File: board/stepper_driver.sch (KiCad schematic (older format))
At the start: 10 parts

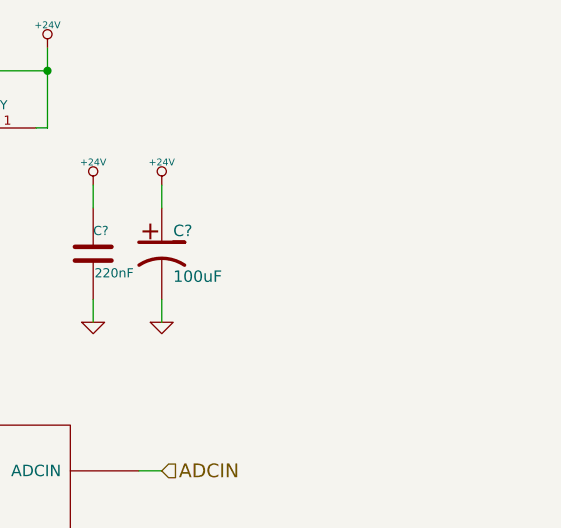
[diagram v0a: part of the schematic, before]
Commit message: Reiner Documentation, Industrial GPIO, Driver Fix
I added documentation for the meaning of Reiner's board pins. I have
finished implemented the industrial inputs on the schematic and partial
industrial outputs. I have added some capacitors to the motor drivers.
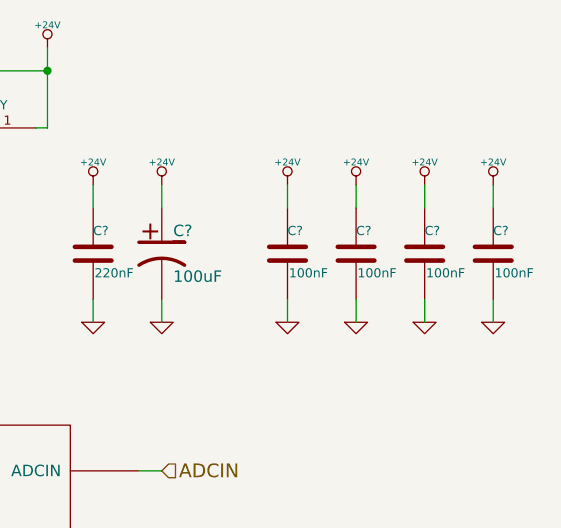
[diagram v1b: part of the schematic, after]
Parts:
- added C? (x4): 100nF, symbol C
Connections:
- net +24V: now also C?.1, C?.1, C?.1, C?.1
- net GND: now also C?.2, C?.2, C?.2, C?.2
- new net: J?.~ (2B), U?.~ (~STBY/RST) (x3)
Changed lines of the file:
@@
 $Descr USLetter 11000 8500
 encoding utf-8
-Sheet 4 10
+Sheet 2 26
 Title "L64470 Stepper Driver"
 Date "21 jan 2014"
@@
 Wire Wire Line
 	6550 3850 6650 3850
+$Comp
+L GND #PWR?
+U 1 1 52FDE021
+P 7200 3200
+F 0 "#PWR?" H 7200 3200 30  0001 C CNN
+F 1 "GND" H 7200 3130 30  0001 C CNN
+F 2 "" H 7200 3200 60  0000 C CNN
+F 3 "" H 7200 3200 60  0000 C CNN
+	1    7200 3200
+	1    0    0    -1
+$EndComp
+$Comp
+L +24V #PWR?
+U 1 1 52FDE027
+P 7200 2600
+F 0 "#PWR?" H 7200 2550 20  0001 C CNN
+F 1 "+24V" H 7200 2700 30  0000 C CNN
+F 2 "" H 7200 2600 60  0000 C CNN
+F 3 "" H 7200 2600 60  0000 C CNN
+	1    7200 2600
+	1    0    0    -1
+$EndComp
+$Comp
+L C C?
+U 1 1 52FDE02D
+P 7200 2900
+F 0 "C?" H 7200 3000 40  0000 L CNN
+F 1 "100nF" H 7206 2815 40  0000 L CNN
+F 2 "" H 7238 2750 30  0000 C CNN
+F 3 "" H 7200 2900 60  0000 C CNN
+	1    7200 2900
+	1    0    0    -1
+$EndComp
+Wire Wire Line
+	7200 2600 7200 2700
+Wire Wire Line
+	7200 3100 7200 3200
+$Comp
+L GND #PWR?
+U 1 1 52FDE03A
+P 7500 3200
+F 0 "#PWR?" H 7500 3200 30  0001 C CNN
+F 1 "GND" H 7500 3130 30  0001 C CNN
+F 2 "" H 7500 3200 60  0000 C CNN
+F 3 "" H 7500 3200 60  0000 C CNN
+	1    7500 3200
+	1    0    0    -1
+$EndComp
+$Comp
+L +24V #PWR?
+U 1 1 52FDE040
+P 7500 2600
+F 0 "#PWR?" H 7500 2550 20  0001 C CNN
+F 1 "+24V" H 7500 2700 30  0000 C CNN
+F 2 "" H 7500 2600 60  0000 C CNN
+F 3 "" H 7500 2600 60  0000 C CNN
+	1    7500 2600
+	1    0    0    -1
+$EndComp
+$Comp
+L C C?
+U 1 1 52FDE046
+P 7500 2900
+F 0 "C?" H 7500 3000 40  0000 L CNN
+F 1 "100nF" H 7506 2815 40  0000 L CNN
+F 2 "" H 7538 2750 30  0000 C CNN
+F 3 "" H 7500 2900 60  0000 C CNN
+	1    7500 2900
+	1    0    0    -1
+$EndComp
+Wire Wire Line
+	7500 2600 7500 2700
+Wire Wire Line
+	7500 3100 7500 3200
+$Comp
+L GND #PWR?
+U 1 1 52FDE04E
+P 7800 3200
+F 0 "#PWR?" H 7800 3200 30  0001 C CNN
+F 1 "GND" H 7800 3130 30  0001 C CNN
+F 2 "" H 7800 3200 60  0000 C CNN
+F 3 "" H 7800 3200 60  0000 C CNN
+	1    7800 3200
+	1    0    0    -1
+$EndComp
+$Comp
+L +24V #PWR?
+U 1 1 52FDE054
+P 7800 2600
+F 0 "#PWR?" H 7800 2550 20  0001 C CNN
+F 1 "+24V" H 7800 2700 30  0000 C CNN
+F 2 "" H 7800 2600 60  0000 C CNN
+F 3 "" H 7800 2600 60  0000 C CNN
+	1    7800 2600
+	1    0    0    -1
+$EndComp
+$Comp
+L C C?
+U 1 1 52FDE05A
+P 7800 2900
+F 0 "C?" H 7800 3000 40  0000 L CNN
+F 1 "100nF" H 7806 2815 40  0000 L CNN
+F 2 "" H 7838 2750 30  0000 C CNN
+F 3 "" H 7800 2900 60  0000 C CNN
+	1    7800 2900
+	1    0    0    -1
+$EndComp
+Wire Wire Line
+	7800 2600 7800 2700
+Wire Wire Line
+	7800 3100 7800 3200
+$Comp
+L GND #PWR?
+U 1 1 52FDE062
+P 8100 3200
+F 0 "#PWR?" H 8100 3200 30  0001 C CNN
+F 1 "GND" H 8100 3130 30  0001 C CNN
+F 2 "" H 8100 3200 60  0000 C CNN
+F 3 "" H 8100 3200 60  0000 C CNN
+	1    8100 3200
+	1    0    0    -1
+$EndComp
+$Comp
+L +24V #PWR?
+U 1 1 52FDE068
+P 8100 2600
+F 0 "#PWR?" H 8100 2550 20  0001 C CNN
+F 1 "+24V" H 8100 2700 30  0000 C CNN
+F 2 "" H 8100 2600 60  0000 C CNN
+F 3 "" H 8100 2600 60  0000 C CNN
+	1    8100 2600
+	1    0    0    -1
+$EndComp
+$Comp
+L C C?
+U 1 1 52FDE06E
+P 8100 2900
+F 0 "C?" H 8100 3000 40  0000 L CNN
+F 1 "100nF" H 8106 2815 40  0000 L CNN
+F 2 "" H 8138 2750 30  0000 C CNN
+F 3 "" H 8100 2900 60  0000 C CNN
+	1    8100 2900
+	1    0    0    -1
+$EndComp
+Wire Wire Line
+	8100 2600 8100 2700
+Wire Wire Line
+	8100 3100 8100 3200
 $EndSCHEMATC

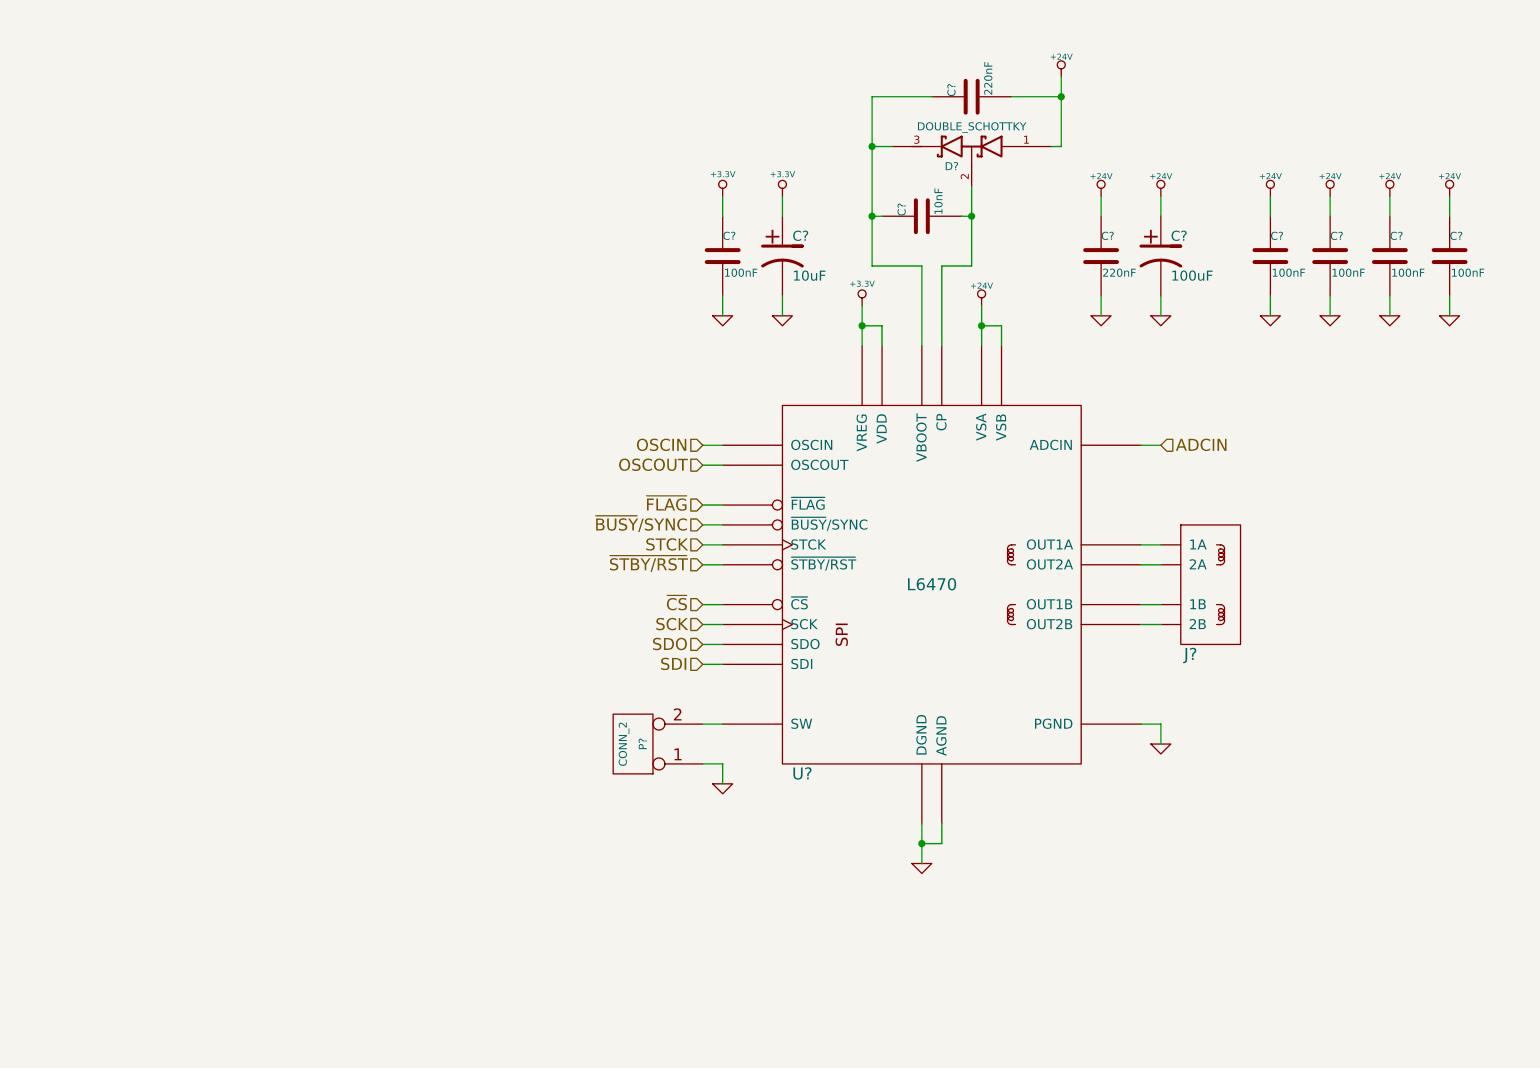
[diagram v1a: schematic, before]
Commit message: Decoupled the Stepper Driver, Main Schematic
The stepper driver is now decoupled according to the demo board
schematic.

The main schematic is nearly complete minus a couple of minor issues.
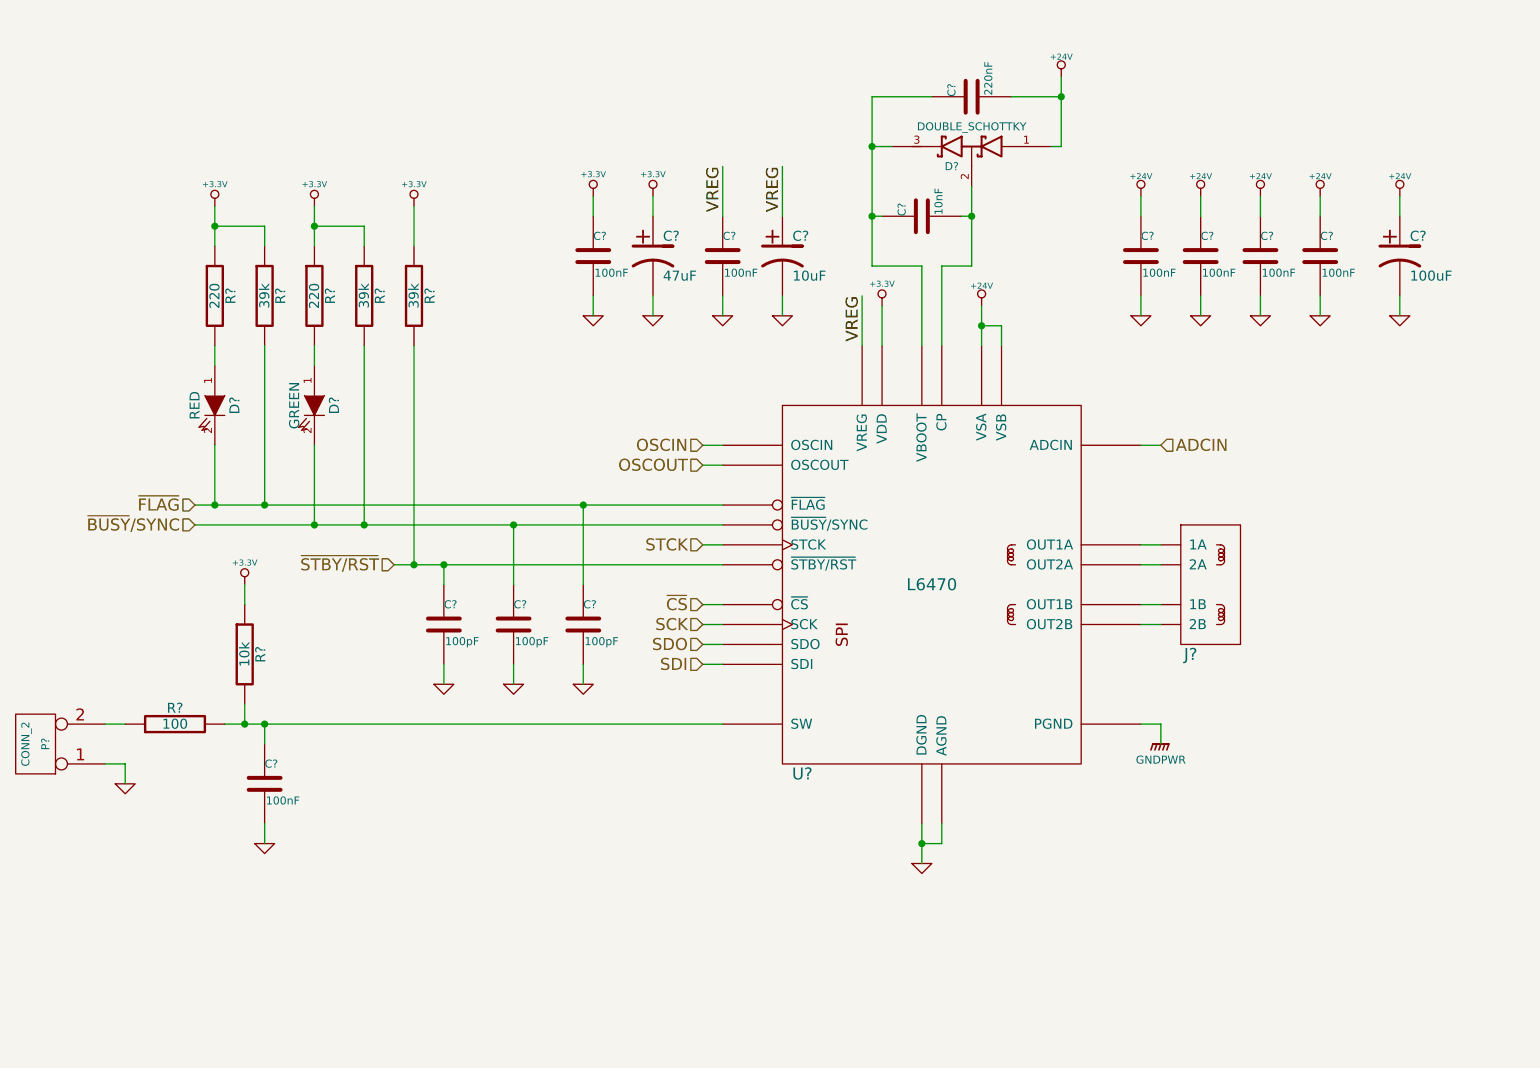
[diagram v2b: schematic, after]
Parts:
- removed C?: 220nF, symbol C
- added C? (x2): 100nF, symbol C
- added C?: 47uF, symbol CP1
- added C? (x3): 100pF, symbol C
- added D?: RED, symbol LED
- added D?: GREEN, symbol LED
- added R? (x2): 220, symbol R
- added R? (x3): 39k, symbol R
- added R?: 10k, symbol R
- added R?: 100, symbol R
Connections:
- net +3.3V: now also C?.1, C?.1, R?.1, R?.1, R?.1, R?.1, R?.1, R?.1; no longer C?.1, C?.1
- net GND: now also C?.2, C?.2, C?.2, C?.2, C?.2, C?.2
- net ~BUSY~/SYNC: now also C?.1, D?.2 (K), R?.2
- net ~FLAG: now also C?.1, D?.2 (K), R?.2
- net ~STBY/RST: now also C?.1, R?.2
- net at P?.2 (PM): now also R?.1; no longer U?.~ (~STBY/RST)
- new net: J?.~ (2B), U?.~ (~STBY/RST) (x3)
- new net: C?.1, R?.2, R?.2, U?.~ (~STBY/RST)
- new net: D?.1 (A), R?.2 (x2)
- new net GNDPWR: U?.~ (~STBY/RST)
- new net VREG: C?.1, C?.1, U?.~ (~STBY/RST)
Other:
- moved on the sheet: C?, P?

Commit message: Made a more efficient use of the MCU hardware peripherals.
See https://github.com/amstan/tr2/wiki/MCU-Pheripherals-Allocation for more details.

* Added STCK pins to individual timers so the MCU can control the steppers step by step.
* Worried about the Industrial GPIOs to be connected to timers(most of them)
* Swapped some SPIs and UARTs to achieve better speeds
* Cleaned up schematic
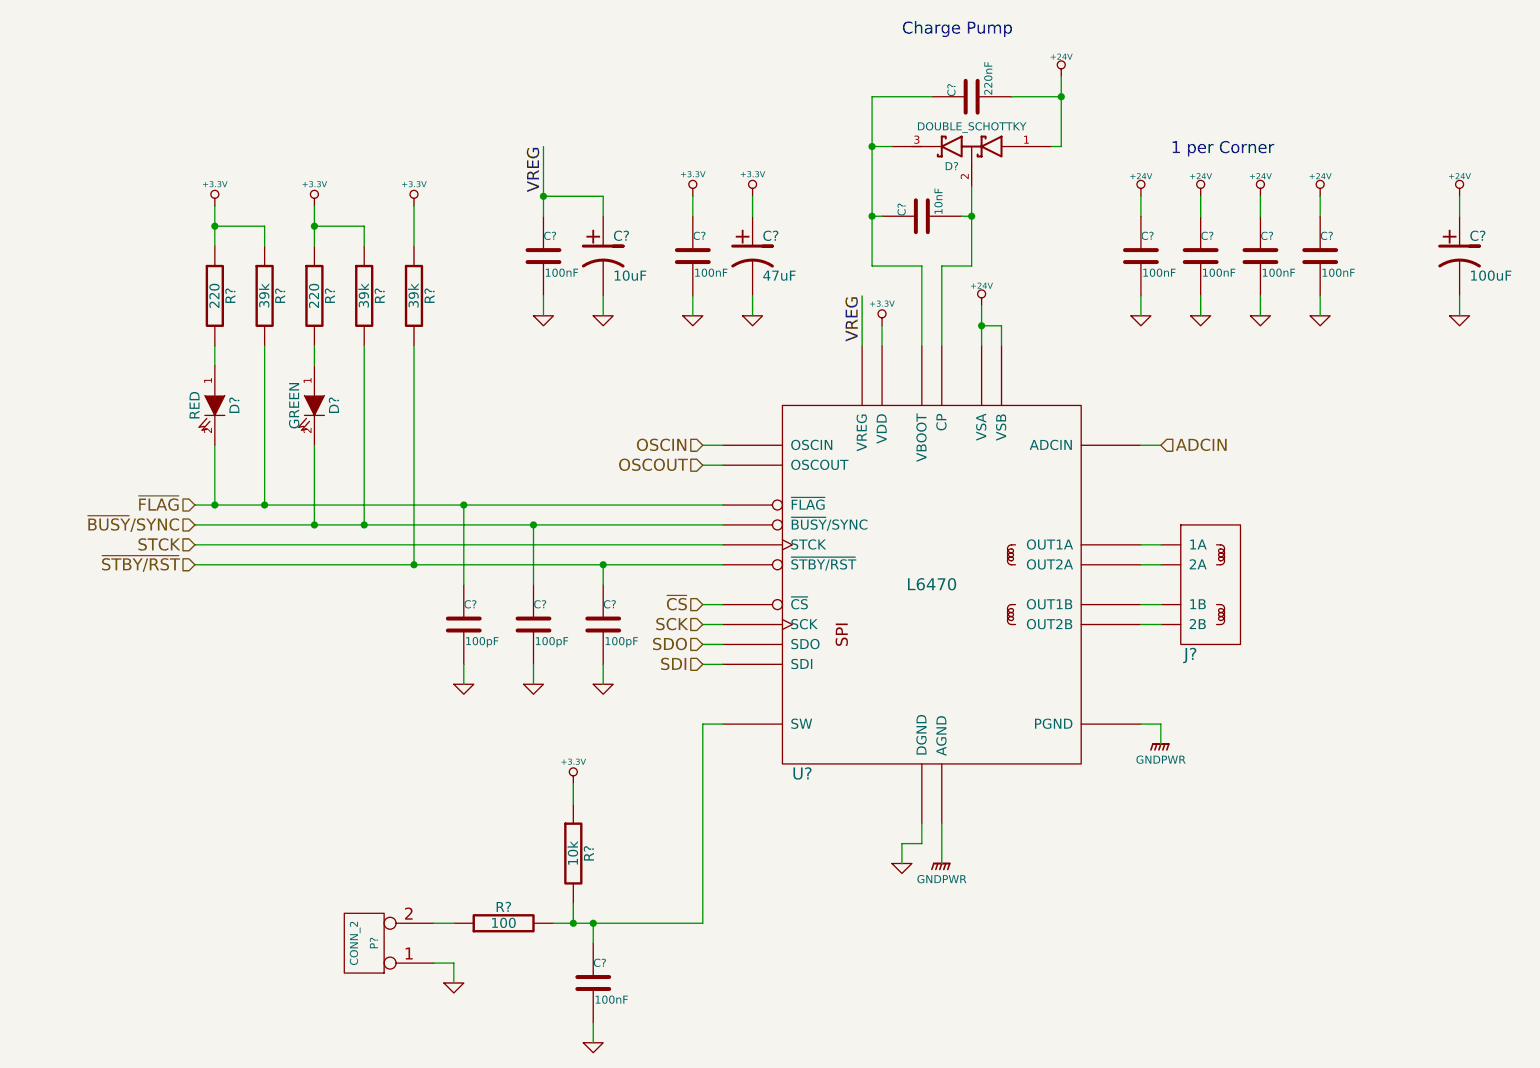
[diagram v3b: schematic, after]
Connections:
- net ~FLAG: now also C?.1; no longer C?.1
- net ~STBY/RST: now also C?.1; no longer C?.1
- new net: J?.~ (2B), U?.~ (~STBY/RST) (x3)
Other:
- note added: "1 per Corner"
- note added: "Charge Pump"
- moved on the sheet: C?, P?, R?

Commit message: Comprehensive Schematic Review, Power LED
The schematic was reviewed. Components were selected. Fixed minor bugs
encountered during review. Debounced switches.

Added a power LED with a transistor that causes it to be normally-on.
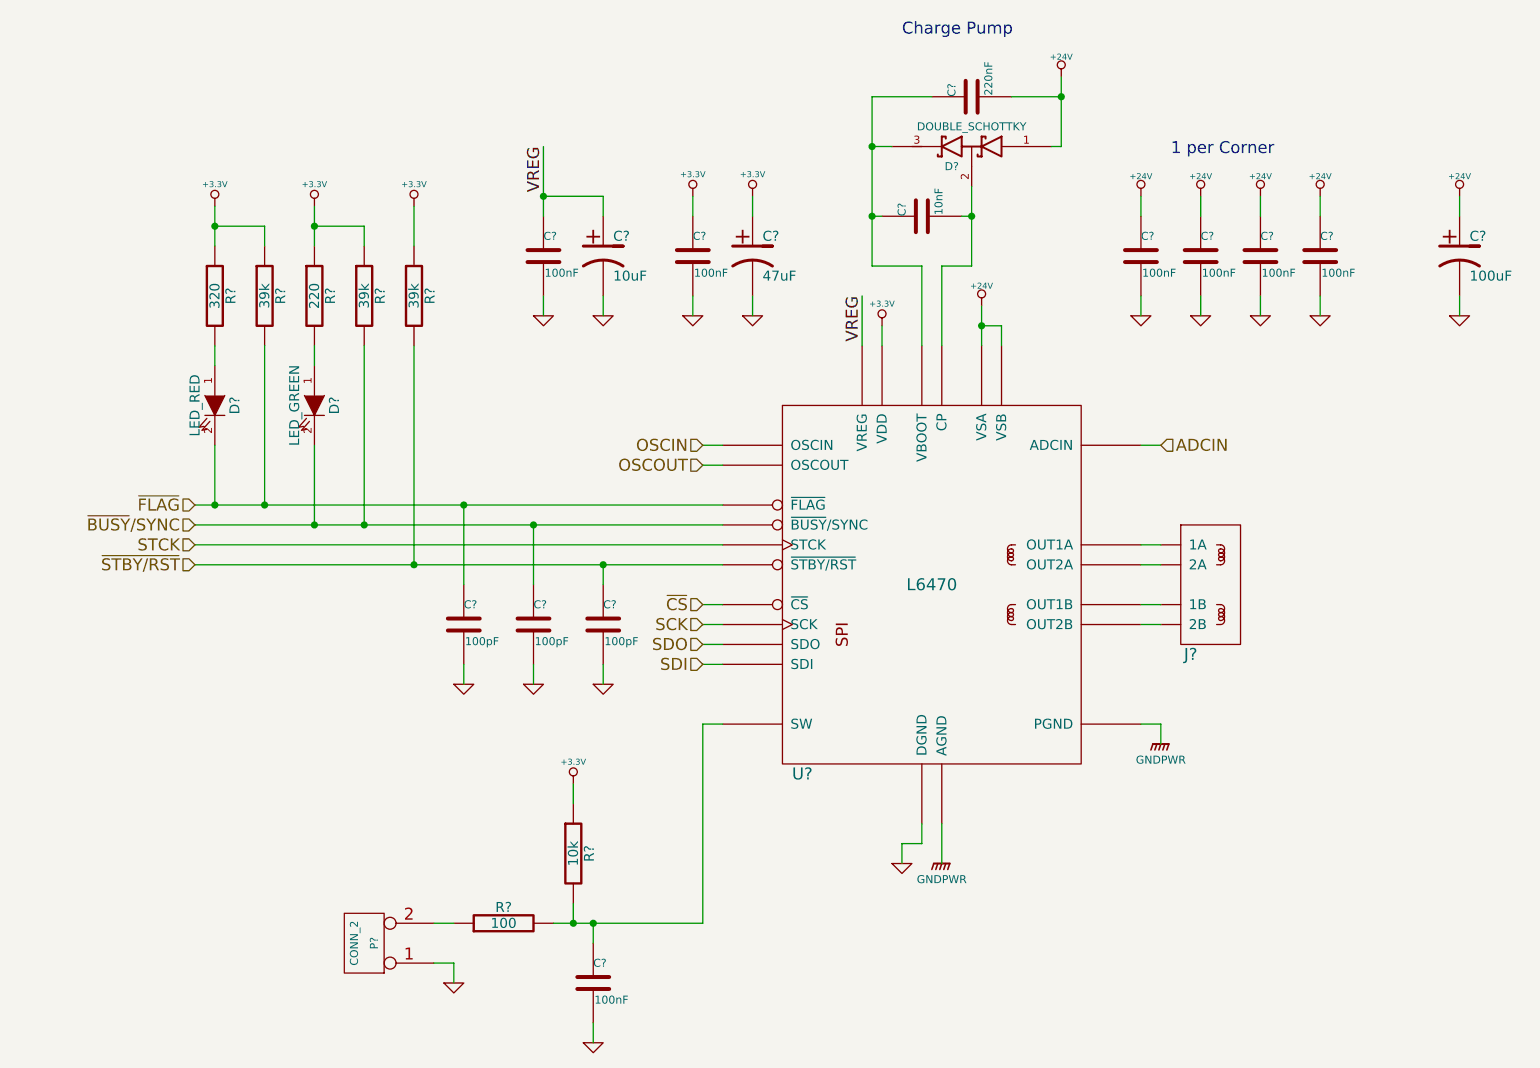
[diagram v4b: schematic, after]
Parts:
- D?: Part Number (none) -> BAS70-04-TP
- D?: value RED -> LED_RED; Part Number (none) -> SML-LX0603SRW-TR
- D?: value GREEN -> LED_GREEN; Part Number (none) -> SML-LX0603SUGW-TR
- R?: value 220 -> 320
- U?: Part Number (none) -> L6470
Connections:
- new net: J?.~ (2B), U?.~ (~STBY/RST) (x3)
